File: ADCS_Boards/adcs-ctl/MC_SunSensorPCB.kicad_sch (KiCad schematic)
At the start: 104 parts, among them J1 PC104_Connector, J2 PPTC062LJBN-RC, J3 Conn_01x03_Female, Q3 20V/0.2A/8MHz/1.2Ω/1Vth, Q4 20V/0.2A/8MHz/1.2Ω/1Vth, U1 9DoF IMU, U10 LM324N, U11 LM324N, U12 LM324N, U13 LM324N, U14 1.8V/100mA, U15 STM32F103RET6, U16 MR25H10MDF, U17 1825232-1, U2 BU33SA5WGWZ-E2, U3 9DoF IMU, U4 DF13-7P-1.25DS(20), U5 DF13-7P-1.25DS(20), U6 DF13-7P-1.25DS(20), U7 DF13-7P-1.25DS(20), U8 LM358N, U9 CD74HC4067M96, Y1 Crystal_GND24

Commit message: adcs: adcs-ctl: clean up MCU schematic, add 3V3 led
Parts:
- removed C1, C24, C27, C30: 1.0uF, SparkFun_IMU_Breakout_ICM-20948:0603, symbol SparkFun_IMU_Breakout_ICM-20948-eagle-import:1.0UF-0603-16V-10%-X7R
- removed C10, C11, C12, C13, C14, C15, C16, C17, C18, C19, C20, C21, C3, C4, C5, C6: 180pF, Capacitor_SMD:C_0603_1608Metric, symbol Device:C
- removed C2, C32, C34, C35, C36, C37, C38, C7, C8, C9: 100nF, Capacitor_SMD:C_0603_1608Metric, symbol Device:C
- removed C22, C23, C28, C29: 0.1uF, SparkFun_IMU_Breakout_ICM-20948:0603, symbol SparkFun_IMU_Breakout_ICM-20948-eagle-import:0.1UF-0603-25V-5%
- removed C25, C26: 4pF, Capacitor_SMD:C_0603_1608Metric, symbol Device:C
- removed C31: 100nF, STM32_Breakout:CAPC1608X90, symbol STM32_Breakout-rescue:CC0603MRX5R5BB475-CC0603MRX5R5BB475
- removed C33: 10uF, Capacitor_SMD:C_0603_1608Metric, symbol Device:C
- removed C39: 10nF, Capacitor_SMD:C_0603_1608Metric, symbol Device:C
- removed C40, C41: 1uF, Capacitor_SMD:C_0603_1608Metric, symbol Device:C
- removed C42, C43: 10uF, SparkFun_IMU_Breakout_ICM-20948:0603, symbol SparkFun_IMU_Breakout_ICM-20948-eagle-import:1.0UF-0603-16V-10%-X7R
- removed D1: RED, SparkFun_IMU_Breakout_ICM-20948:LED-0603, symbol SparkFun_IMU_Breakout_ICM-20948-eagle-import:LED-RED0603
- removed D3: RED, LED_SMD:LED_0603_1608Metric_Pad1.05x0.95mm_HandSolder, symbol Device:LED_Small
- removed FB1: 100R @ 100 MHz, STM32_Breakout:INDUC1607X60N, symbol Device:Ferrite_Bead_Small
- removed FB2: FerriteBead, Inductor_SMD:L_0603_1608Metric, symbol Device:FerriteBead
- removed H1, H2, H3, H4: MountingHole_Pad, MountingHole:MountingHole_3.2mm_M3_Pad_TopBottom, symbol Mechanical:MountingHole_Pad
- removed J1: PC104_Connector, pc104-connector:pc104-connector, symbol qset-connector-library:PC104_Connector
- removed J2: PPTC062LJBN-RC, Connector_PinSocket_2.54mm:PinSocket_2x06_P2.54mm_Horizontal, symbol ADCS_Symbols:PPTC062LJBN-RC
- removed J3: Conn_01x03_Female, Footprints_QSAT:1x3_Connector_Female, symbol Connector:Conn_01x03_Female
- removed Q3, Q4: 20V/0.2A/8MHz/1.2Ω/1Vth, SparkFun_IMU_Breakout_ICM-20948:SOT-416FL, symbol SparkFun_IMU_Breakout_ICM-20948-eagle-import:MOSFET-NCH-RE1C002UN
- removed R10, R11, R12, R13, R14, R15, R16, R17, R18, R19, R20, R21, R22, R23, R24, R9: 5.76k, Resistor_SMD:R_0603_1608Metric, symbol Device:R
- removed R2: 10k, Resistor_SMD:R_0603_1608Metric, symbol Device:R
- removed R26, R27, R28, R29: 2.2k, SparkFun_IMU_Breakout_ICM-20948:0402-TIGHT, symbol SparkFun_IMU_Breakout_ICM-20948-eagle-import:2.2KOHM-0402T-1/16W-1%
- removed R36: 220, SparkFun_IMU_Breakout_ICM-20948:0603, symbol SparkFun_IMU_Breakout_ICM-20948-eagle-import:220OHM-0603-1/10W-1%
- removed R53: 2k2, STM32_Breakout:RESC1607X60N, symbol STM32_Breakout-rescue:R0603-OBC_Libary
- removed R54, R55: 10k, STM32_Breakout:RESC1607X60N, symbol STM32_Breakout-rescue:R0603-OBC_Libary
- removed R7: 1Meg, Resistor_SMD:R_0603_1608Metric, symbol Device:R
- removed R8: 2Meg, Resistor_SMD:R_0603_1608Metric, symbol Device:R
- removed S1: TL3305CF260QG, Footprints_QSAT:SW_TL3305CF260QG, symbol ADCS_Symbols:TL3305CF260QG
- removed TP1: 1.8V, SparkFun_IMU_Breakout_ICM-20948:PAD.03X.03, symbol SparkFun_IMU_Breakout_ICM-20948-eagle-import:TEST-POINT3
- removed TP2: 3V3, SparkFun_IMU_Breakout_ICM-20948:PAD.03X.03, symbol SparkFun_IMU_Breakout_ICM-20948-eagle-import:TEST-POINT3
- removed U1, U3: 9DoF IMU, SparkFun_IMU_Breakout_ICM-20948:QFN24-3X3, symbol SparkFun_IMU_Breakout_ICM-20948-eagle-import:ICM-20948
- removed U10, U11, U12, U13: LM324N, Footprints_QSAT:Op-Amp, symbol UpdatedControllerBoardSchematic-rescue:Op-Amp
- removed U14: 1.8V/100mA, SparkFun_IMU_Breakout_ICM-20948:SC70, symbol SparkFun_IMU_Breakout_ICM-20948-eagle-import:V_REG_SP6214-1.8V
- removed U15: STM32F103RET6, Footprints_QSAT:QFP50P1200X1200X160-64N, symbol ADCS_Symbols:STM32F103RET6
- removed U16: MR25H10MDF, STM32_Breakout:SON65P300X300X95-8N, symbol STM32_Breakout-rescue:MR25H10MDF-MRAM_Symbol
- removed U17: 1825232-1, Footprints_QSAT:1825232-1, symbol ADCS_Symbols:1825232-1
- removed U2: BU33SA5WGWZ-E2, Footprints_QSAT:BU33SA5WGWZ-E2, symbol qsat5to3.3-rescue:BU33SA5WGWZ-E2-qsat-symb
- removed U4, U5, U6, U7: DF13-7P-1.25DS(20), Connector_Hirose:Hirose_DF13-07P-1.25DS_1x07_P1.25mm_Horizontal, symbol ADCS_Symbols:DF13-4P-1.25DS(20)
- removed U8: LM358N, Footprints_QSAT:DIP794W45P254L959H508Q8, symbol LM358:LM358
- removed U9: CD74HC4067M96, Footprints_QSAT:SOIC127P1030X265-24N, symbol Mux16_1:CD74HC4067M96
- removed Y1: Crystal_GND24, Crystal:Crystal_SMD_3225-4Pin_3.2x2.5mm, symbol Device:Crystal_GND24
- added C?: 1.0uF, Resistor_SMD:R_0603_1608Metric, symbol SparkFun_IMU_Breakout_ICM-20948-eagle-import:1.0UF-0603-16V-10%-X7R
- added C? (x4): 0.1uF, Capacitor_SMD:C_0603_1608Metric, symbol SparkFun_IMU_Breakout_ICM-20948-eagle-import:0.1UF-0603-25V-5%
- added C? (x16): 180pF, Capacitor_SMD:C_0603_1608Metric, symbol Device:C
- added C?: 10uF, Capacitor_SMD:C_0603_1608Metric, symbol Device:C
- added C? (x2): 10uF, SparkFun_IMU_Breakout_ICM-20948:0603, symbol SparkFun_IMU_Breakout_ICM-20948-eagle-import:1.0UF-0603-16V-10%-X7R
- added C? (x2): 4pF, Capacitor_SMD:C_0603_1608Metric, symbol Device:C
- added C? (x10): 100nF, Capacitor_SMD:C_0603_1608Metric, symbol Device:C
- added C? (x2): 1uF, Capacitor_SMD:C_0603_1608Metric, symbol Device:C
- added C?: 10nF, Capacitor_SMD:C_0603_1608Metric, symbol Device:C
- added C?: 100nF, STM32_Breakout:CAPC1608X90, symbol STM32_Breakout-rescue:CC0603MRX5R5BB475-CC0603MRX5R5BB475
- added C? (x2): 1.0uF, Capacitor_SMD:C_0603_1608Metric, symbol SparkFun_IMU_Breakout_ICM-20948-eagle-import:1.0UF-0603-16V-10%-X7R
- added C?: 10uF, Capacitor_SMD:C_0603_1608Metric, symbol SparkFun_IMU_Breakout_ICM-20948-eagle-import:1.0UF-0603-16V-10%-X7R
- added D? (x2): RED, LED_SMD:LED_0603_1608Metric, symbol SparkFun_IMU_Breakout_ICM-20948-eagle-import:LED-RED0603
- added D?: RED, LED_SMD:LED_0603_1608Metric_Pad1.05x0.95mm_HandSolder, symbol Device:LED_Small
- added FB?: 100R @ 100 MHz, STM32_Breakout:INDUC1607X60N, symbol Device:Ferrite_Bead_Small
- added FB?: FerriteBead, Inductor_SMD:L_0603_1608Metric, symbol Device:FerriteBead
- added H? (x4): MountingHole_Pad, MountingHole:MountingHole_3.2mm_M3_Pad_TopBottom, symbol Mechanical:MountingHole_Pad
- added J?: PPTC062LJBN-RC, Connector_PinSocket_2.54mm:PinSocket_2x06_P2.54mm_Horizontal, symbol ADCS_Symbols:PPTC062LJBN-RC
- added J?: PC104_Connector, pc104-connector:pc104-connector, symbol qset-connector-library:PC104_Connector
- added J?: Conn_01x03_Female, Footprints_QSAT:1x3_Connector_Female, symbol Connector:Conn_01x03_Female
- added Q? (x2): 20V/0.2A/8MHz/1.2Ω/1Vth, SparkFun_IMU_Breakout_ICM-20948:SOT-416FL, symbol SparkFun_IMU_Breakout_ICM-20948-eagle-import:MOSFET-NCH-RE1C002UN
- added R? (x2): 2k2, Resistor_SMD:R_0603_1608Metric, symbol SparkFun_IMU_Breakout_ICM-20948-eagle-import:220OHM-0603-1/10W-1%
- added R? (x4): 2.2k, SparkFun_IMU_Breakout_ICM-20948:0402-TIGHT, symbol SparkFun_IMU_Breakout_ICM-20948-eagle-import:2.2KOHM-0402T-1/16W-1%
- added R? (x16): 5.76k, Resistor_SMD:R_0603_1608Metric, symbol Device:R
- added R?: 2Meg, Resistor_SMD:R_0603_1608Metric, symbol Device:R
- added R?: 1Meg, Resistor_SMD:R_0603_1608Metric, symbol Device:R
- added R?: 10k, Resistor_SMD:R_0603_1608Metric, symbol Device:R
- added R?: 2k2, STM32_Breakout:RESC1607X60N, symbol STM32_Breakout-rescue:R0603-OBC_Libary
- added R?: 10k, STM32_Breakout:RESC1607X60N, symbol STM32_Breakout-rescue:R0603-OBC_Libary
- added R?: 10k, Resistor_SMD:R_0603_1608Metric, symbol STM32_Breakout-rescue:R0603-OBC_Libary
- added S?: TL3305CF260QG, Footprints_QSAT:SW_TL3305CF260QG, symbol ADCS_Symbols:TL3305CF260QG
- added TP?: 1V8, TestPoint:TestPoint_THTPad_2.0x2.0mm_Drill1.0mm, symbol SparkFun_IMU_Breakout_ICM-20948-eagle-import:TEST-POINT3
- added TP?: 3V3, TestPoint:TestPoint_THTPad_2.0x2.0mm_Drill1.0mm, symbol SparkFun_IMU_Breakout_ICM-20948-eagle-import:TEST-POINT3
- added U?: MR25H10MDF, STM32_Breakout:SON65P300X300X95-8N, symbol STM32_Breakout-rescue:MR25H10MDF-MRAM_Symbol
- added U? (x4): LM324N, Footprints_QSAT:Op-Amp, symbol UpdatedControllerBoardSchematic-rescue:Op-Amp
- added U?: 1825232-1, Footprints_QSAT:1825232-1, symbol ADCS_Symbols:1825232-1
- added U? (x4): DF13-7P-1.25DS(20), Connector_Hirose:Hirose_DF13-07P-1.25DS_1x07_P1.25mm_Horizontal, symbol ADCS_Symbols:DF13-4P-1.25DS(20)
- added U?: STM32F103RET6, Footprints_QSAT:QFP50P1200X1200X160-64N, symbol ADCS_Symbols:STM32F103RET6
- added U?: BU33SA5WGWZ-E2, qset-footprints:BU33SA5WGWZ-E2, symbol qsat5to3.3-rescue:BU33SA5WGWZ-E2-qsat-symb
- added U?: CD74HC4067M96, Footprints_QSAT:SOIC127P1030X265-24N, symbol Mux16_1:CD74HC4067M96
- added U? (x2): 9DoF IMU, SparkFun_IMU_Breakout_ICM-20948:QFN24-3X3, symbol SparkFun_IMU_Breakout_ICM-20948-eagle-import:ICM-20948
- added U?: 1.8V/100mA, SparkFun_IMU_Breakout_ICM-20948:SC70, symbol SparkFun_IMU_Breakout_ICM-20948-eagle-import:V_REG_SP6214-1.8V
- added U?: LM358N, Footprints_QSAT:DIP794W45P254L959H508Q8, symbol LM358:LM358
- added Y?: Crystal_GND24, Crystal:Crystal_SMD_3225-4Pin_3.2x2.5mm, symbol Device:Crystal_GND24
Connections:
- net +3.3VA: now also C?.1, C?.1, FB?.1, U?.13 (VDDA)
- net +3V3: now also C?.1, C?.1, C?.1, C?.1, C?.1, C?.1, C?.1, C?.2, D?.2 (A), D?.A, FB?.1, FB?.2, J?.7, R?.1, R?.2, R?.2, R?.2, TP?.P$1 (1), U?.1 (VBAT), U?.19 (VDD_4), U?.3, U?.32 (VDD_1), U?.48 (VDD_2), U?.64 (VDD_3), U?.~ (Vout)
- net +5V: now also C?.1, C?.1, C?.1, C?.1, C?.1, C?.1, J?.78 (H1-26), U?.1 (IN), U?.24 (VCC), U?.3 (EN), U?.3 (Input), U?.4, U?.4, U?.4, U?.4, U?.8 (V+)
- net 1.8V: now also C?.1, C?.1, C?.1, C?.1, C?.1, D?.A, Q?.1 (G), Q?.1 (G), R?.2, R?.2, TP?.P$1 (1), U?.13 (VDD), U?.13 (VDD), U?.5 (OUT), U?.8 (VDDIO), U?.8 (VDDIO), U?.9 (AD0/SDO)
- net BOOT0: now also R?.2, U?.60 (BOOT0)
- net GND: now also C?.1, C?.2, C?.2, C?.2, C?.2, C?.2, C?.2, C?.2, C?.2, C?.2, C?.2, C?.2, C?.2, C?.2, C?.2, C?.2, C?.2, C?.2, C?.2, C?.2, C?.2, C?.2, C?.2, C?.2, C?.2, C?.2, C?.2, J?.100 (H2-48), J?.61 (H2-9), J?.66 (H1-14), J?.69 (H2-17), J?.73 (H2-21), J?.74 (H1-22), J?.8, J?.81 (H2-29), J?.82 (H1-30), J?.84 (H1-32), J?.99 (H2-47), R?.1, R?.1, R?.2, R?.2, S?.3, S?.4, U?.1, U?.1 (GND), U?.10, U?.10, U?.10, U?.10, U?.11, U?.11, U?.11, U?.11, U?.12, U?.12, U?.12, U?.12, U?.12 (GND), U?.12 (VSSA), U?.18 (GND), U?.18 (GND), U?.18 (VSS_4), U?.2, U?.2, U?.2, U?.2, U?.2 (GND), U?.20 (GND), U?.20 (GND), U?.3, U?.3, U?.3, U?.3, U?.31 (VSS_1), U?.4, U?.4, U?.4, U?.4, U?.4 (GND), U?.4 (VSS), U?.47 (VSS_2), U?.5, U?.5, U?.5, U?.5, U?.6, U?.6, U?.6, U?.6, U?.63 (VSS_3), U?.9 (AD0/SDO), U?.9 (Sink), Y?.2, Y?.4
- net GPIO1: now also R?.2, U?.24 (PC4/ADC12_IN14), U?.7 (HOLD)
- net GPIO2: now also R?.1, U?.25 (PC5/ADC12_IN15), U?.3 (WP)
- net IMU_SCL: now also Q?.3 (D), R?.1, U?.39 (PC8/TIM8_CH3/SDIO_D0/TIM3_CH3)
- net IMU_SDA: now also Q?.3 (D), R?.1, U?.40 (PC9/TIM8_CH4/SDIO_D1/TIM3_CH4)
- net MuxEnable: now also U?.14 (PA0-WKUP/USART2_CTS/ADC123_IN0/TIM2_CH1_ETR/TIM5_CH1/TIM8_ETR), U?.15 (~{E})
- net MuxOut: now also U?.1, U?.2, U?.21 (PA5/SPI1_SCK/DAC_OUT2/ADC12_IN5)
- net MuxOut_1: now also R?.1, U?.1 (COM_I/O)
- net MuxS0: now also U?.10 (S0), U?.15 (PA1/USART2_RTS/ADC123_IN1/TIM5_CH2/TIM2_CH2)
- net MuxS1: now also U?.11 (S1), U?.16 (PA2/USART2_TX/TIM5_CH3/ADC123_IN2/TIM2_CH3)
- net MuxS2: now also U?.14 (S2), U?.17 (PA3/USART2_RX/TIM5_CH4/ADC123_IN3/TIM2_CH4)
- net MuxS3: now also U?.13 (S3), U?.20 (PA4/SPI1_NSS/USART2_CK/DAC_OUT1/ADC12_IN4)
- net NRST: now also C?.1, S?.1, S?.2, U?.7 (NRST)
- net PA10: now also J?.20 (H1-20), U?.43 (PA10/USART1_RX/TIM1_CH3)
- net PA11: now also J?.21 (H1-21), U?.44 (PA11/USART1_CTS/USBDMCAN_RX/TIM1_CH4)
- net PA12: now also J?.22 (H1-22), U?.45 (PA12/USART1_RTS/USBDP/CAN_TX/TIM1_ETR)
- net PA15: now also J?.25 (H1-25), U?.50 (PA15/SPI3_NSS/I2S3_WS)
- net PA6: now also J?.16 (H1-16), U?.22 (PA6/SPI1_MISO/TIM8_BKIN/ADC12_IN6/TIM3_CH1)
- net PA7: now also J?.17 (H1-17), U?.23 (PA7/SPI1_MOSI/TIM8_CH1N/ADC12_IN7/TIM3_CH2)
- net PA8: now also J?.18 (H1-18), U?.41 (PA8/USART1_CK/TIM1_CH1/MCO)
- net PA9: now also J?.19 (H1-19), U?.42 (PA9/USART1_TX/TIM1_CH2)
- net PB0: now also J?.24 (H1-24), U?.26 (PB0/ADC12_IN8/TIM3_CH3/TIM8_CH2N)
- net PB1: now also J?.42 (H1-42), U?.27 (PB1/ADC12_IN9/TIM3_CH4/TIM8_CH3N)
- net PB10: now also J?.23 (H1-23), U?.29 (PB10/I2C2_SCL/USART3_TX/TIM2_CH3)
- net PB11: now also J?.51 (H1-51), U?.30 (PB11/2C2_SDA/USART3_RX/TIM2_CH4)
- net PB12: now also J?.26 (H1-26), U?.33 (PB12/SPI2_NSS/I2S2_WS/I2C2_SMBA/USART3_CK/TIM1_BKIN)
- net PB13: now also J?.27 (H1-27), U?.34 (PB13/SPI2_SCK/I2S2_CK/USART3_CTS/TIM1_CH1N)
- net PB14: now also J?.37 (H1-37), U?.35 (PB14/SPI2_MISO/TIM1_CH2N/USART3_RTS)
- net PB15: now also J?.38 (H1-38), U?.36 (PB15/SPI2_MOSI/I2S2_SD/TIM1_CH3N)
- net PB2: now also U?.28 (PB2//BOOT1)
- net PB4: now also J?.50 (H1-50), U?.56 (PB4/SPI3_MISO/TIM3_CH1/SPI1_MISO)
- net PB5: now also U?.57 (PB5/TIM3_CH2/SPI1_MOSI/)
- net PB8: now also J?.52 (H1-52), U?.61 (PB8/TIM4_CH3/SDIO_D4/I2C1_SCL/CAN_RX)
- net PB9: now also U?.62 (PB9/TIM4_CH4/SDIO_D5/I2C1_SDA/CAN_TX)
- net PC10: now also J?.5 (H1-5), U?.51 (PC10/UART4_TX/SDIO_D2/USART3_TX)
- net PC11: now also J?.44 (H1-44), U?.52 (PC11/UART4_RX/SDIO_D3/USART3_RX)
- net PC12: now also J?.45 (H1-45), U?.53 (PC12/UART5_TX/SDIO_CK/USART3_CK)
- net PC13: now also J?.46 (H1-46), U?.2 (PC13-TAMPER-RTC)
- net PC14: now also J?.47 (H1-47), U?.3 (PC14-OSC32_IN)
- net PC15: now also J?.48 (H1-48), U?.4 (PC15-OSC32_OUT)
- net PC6: now also J?.39 (H1-39), U?.37 (PC6/I2S2_MCK/TIM8_CH1/SDIO_D6/TIM3_CH1)
- net PC7: now also J?.40 (H1-40), U?.38 (PC7/I2S3_MCK/TIM8_CH2/SDIO_D7/TIM3_CH2)
- net PD1_O1: now also C?.2, R?.2, U?.1, U?.2
- net PD1_O2: now also C?.2, R?.2, U?.1, U?.2
- net PD1_O3: now also C?.2, R?.2, U?.1, U?.2
- net PD1_O4: now also C?.2, R?.2, U?.1, U?.2
- net PD2: now also J?.49 (H1-49), U?.54 (PD2/TIM3_ETR/UART5_RX/SDIO_CMD)
- net PD2_O1: now also C?.2, R?.1, U?.3, U?.6
- net PD2_O2: now also C?.2, R?.1, U?.3, U?.6
- net PD2_O3: now also C?.2, R?.1, U?.3, U?.6
- net PD2_O4: now also C?.2, R?.1, U?.3, U?.6
- net PD3_O1: now also C?.2, R?.2, U?.13, U?.5
- net PD3_O2: now also C?.2, R?.2, U?.13, U?.5
- net PD3_O3: now also C?.2, R?.2, U?.13, U?.5
- net PD3_O4: now also C?.2, R?.2, U?.13, U?.5
- net PD4_O1: now also C?.1, R?.1, U?.7, U?.9
- net PD4_O2: now also C?.1, R?.1, U?.7, U?.9
- net PD4_O3: now also C?.1, R?.1, U?.7, U?.9
- net PD4_O4: now also C?.1, R?.1, U?.7, U?.9
- net SPI1_MISO: now also U?.11 (PC3/ADC123_IN13), U?.2 (SO)
- net SPI1_MOSI: now also U?.5 (SI), U?.9 (PC1/ADC123_IN11)
- net SPI1_NSS: now also U?.1 (CS), U?.10 (PC2/ADC123_IN12)
- net SPI1_SCK: now also U?.6 (SCK), U?.8 (PC0/ADC123_IN10)
- net SW_BOOT0: now also R?.1, U?.2
- net SYS_JTCK-SWCLK: now also J?.2 (Pin_2), U?.49 (PA14/JTCKSWCLK)
- net SYS_JTDO-TRACESWO: now also J?.3 (Pin_3), U?.55 (PB3/SPI3_SCK/I2S3_CK/TRACESWO/TIM2_CH2/SPI1_SCK)
- net SYS_JTMS-SWDIO: now also J?.1 (Pin_1), U?.46 (PA13/JTMSSWDIO)
- new net: D?.C, R?.2 (x2)
- new net: C?.1, FB?.2, U?.8 (VDD)
- new net: C?.1, R?.2, U?.7, U?.8 (I1)
- new net: C?.1, R?.1, U?.14, U?.3 (I6)
- new net: C?.2, R?.2, U?.20 (I11), U?.8
- new net: R?.1, R?.2, U?.3
- new net: C?.1, R?.1, U?.1, U?.19 (I12)
- new net: C?.1, R?.1, U?.14, U?.21 (I10)
- new net: C?.1, R?.2, U?.4 (I5), U?.7
- new net: C?.1, R?.1, U?.1, U?.5 (I4)
- new net: C?.2, R?.2, U?.2 (I7), U?.8
- new net: C?.1, R?.1, U?.14, U?.17 (I14)
- new net: C?.2, R?.2, U?.16 (I15), U?.8
- new net: C?.1, U?.5 (PD0-OSC_IN/FSMC_D2/CAN_RX), Y?.3
- new net: C?.1, U?.6 (PD1-OSC_OUT/FSMC_D3/CAN_TX), Y?.1
- new net: C?.1, R?.2, U?.18 (I13), U?.7
- new net: C?.1, R?.1, U?.14, U?.7 (I2)
- new net: C?.1, R?.2, U?.22 (I9), U?.7
- new net: C?.2, R?.2, U?.6 (I3), U?.8
- new net: C?.1, R?.1, U?.1, U?.9 (I0)
- new net: C?.1, R?.1, U?.1, U?.23 (I8)
- new net: C?.1, U?.10 (REGOUT) (x2)
- new net: D?.1 (K), R?.1
- new net I2C1_SCL: J?.11, J?.43 (H1-43), U?.58 (PB6/I2C1_SCL/TIM4_CH1/USART1_TX)
- new net I2C1_SDA: J?.12, J?.41 (H1-41), U?.59 (PB7/I2C1_SDA/FSMC_NADV/TIM4_CH2/USART1_RX)
- new net IMU_SCL_1V8: Q?.2 (S), R?.1, U?.23 (SCL/SCLK), U?.23 (SCL/SCLK)
- new net IMU_SDA_1V8: Q?.2 (S), R?.1, U?.24 (SDA/SDI), U?.24 (SDA/SDI)
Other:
- note added: "1V8 I2C Pullups"
- note added: "1V8 Power Generation"
- note added: "3V3 Power Generation"
- note added: "MCU - STM32F103RET6"
- note added: "PMOD Test Connector"
- note added: "SWD / Programming Header"
- note removed: "1v8 Power Generation"
- note removed: "3v3 Power Generation"
- note removed: "Crystal Oscillator"
- note removed: "I2C Pullups"
- note removed: "PMOD"
- note removed: "SWD"

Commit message: adcs: adcs-ctl: change boot switch to standard footprint and symbol
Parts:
- removed U?: 1825232-1, Footprints_QSAT:1825232-1, symbol ADCS_Symbols:1825232-1
- added SW1: SW_SPDT, Button_Switch_SMD:SW_SPDT_PCM12, symbol Switch:SW_SPDT
- gave numbers to parts that had none: 105
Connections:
- net +3V3: now also SW1.3 (C)
- net GND: now also SW1.1 (A)
- net SW_BOOT0: now also SW1.2 (B)

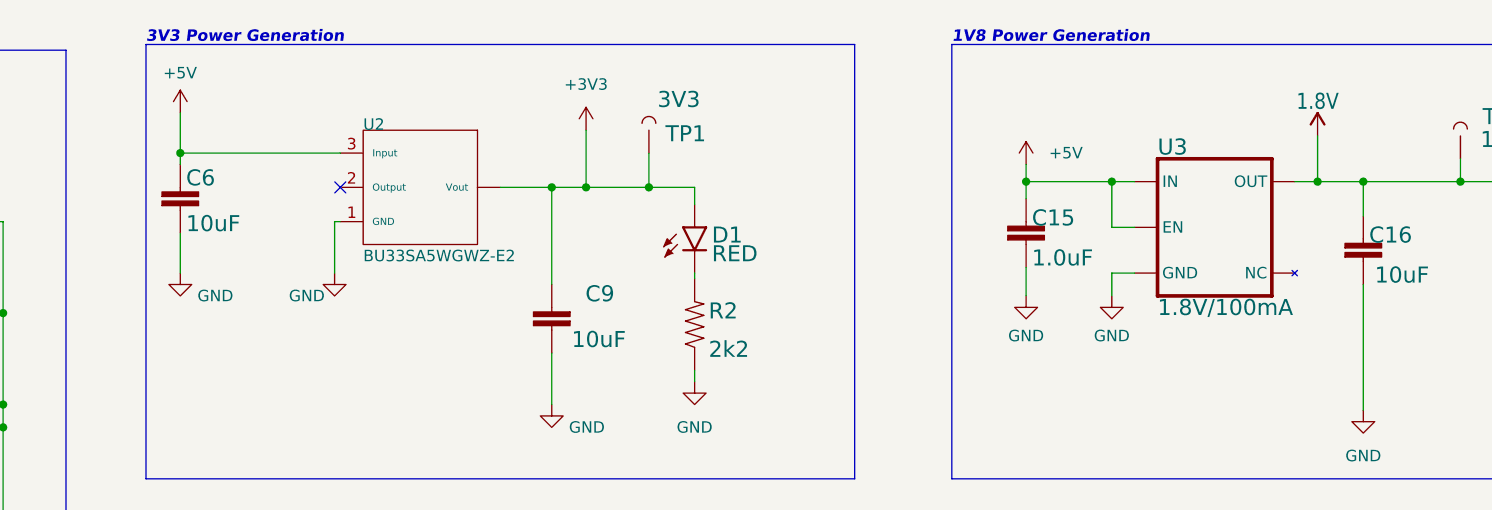
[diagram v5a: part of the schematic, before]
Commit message: adcs: adcs-ctl: use AMS1117 regulators
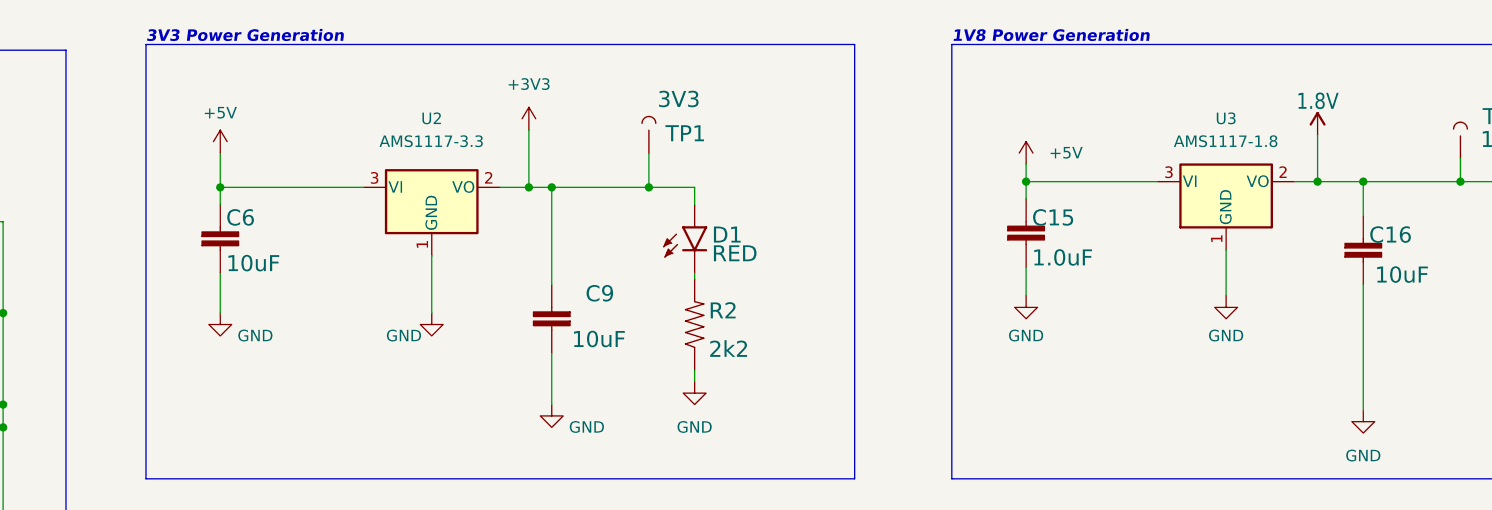
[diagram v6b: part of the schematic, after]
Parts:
- removed U2: BU33SA5WGWZ-E2, qset-footprints:BU33SA5WGWZ-E2, symbol qsat5to3.3-rescue:BU33SA5WGWZ-E2-qsat-symb
- removed U3: 1.8V/100mA, SparkFun_IMU_Breakout_ICM-20948:SC70, symbol SparkFun_IMU_Breakout_ICM-20948-eagle-import:V_REG_SP6214-1.8V
- added U2: AMS1117-3.3, Package_TO_SOT_SMD:SOT-223-3_TabPin2, symbol Regulator_Linear:AMS1117-3.3
- added U3: AMS1117-1.8, Package_TO_SOT_SMD:SOT-223-3_TabPin2, symbol Regulator_Linear:AMS1117-1.8
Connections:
- net +3V3: now also U2.2 (VO)
- net +5V: now also U2.3 (VI), U3.3 (VI)
- net 1.8V: now also U3.2 (VO)
- net GND: now also U2.1 (GND), U3.1 (GND)
- no-connect marks 78 -> 77
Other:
- moved on the sheet: C6

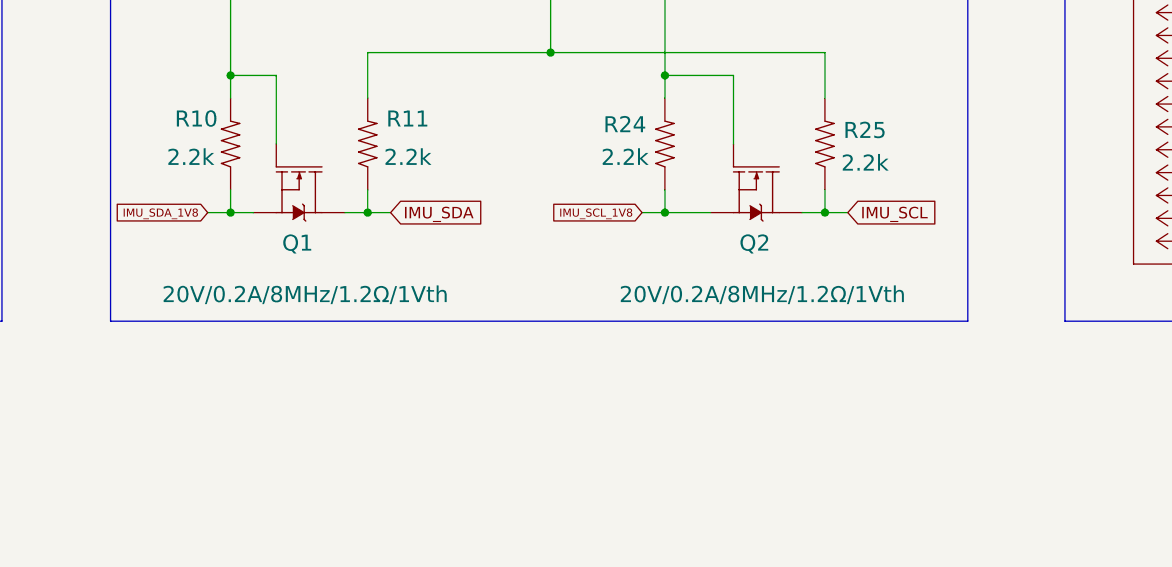
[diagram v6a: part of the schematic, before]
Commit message: adcs: adcs-ctl: use re1c002unctl transistors over SparkFun transistors
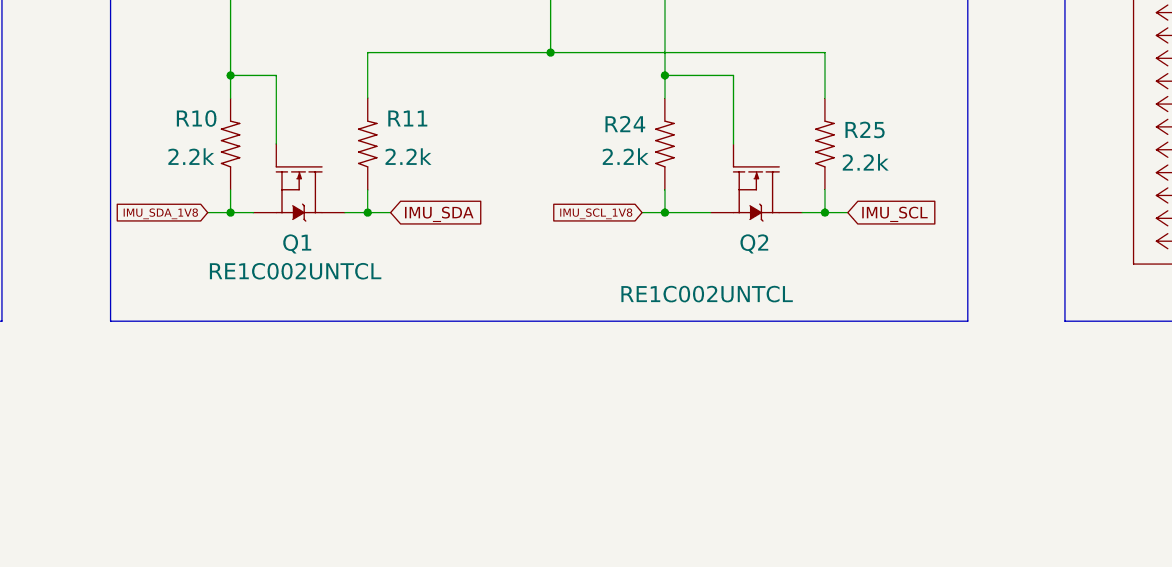
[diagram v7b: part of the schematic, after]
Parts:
- Q1, Q2: value 20V/0.2A/8MHz/1.2Ω/1Vth -> RE1C002UNTCL; footprint SparkFun_IMU_Breakout_ICM-20948:SOT-416FL -> qset-footprints:RE1C002UNTCL
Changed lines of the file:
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@@
       (effects (font (size 1.778 1.778)) (justify left bottom))
     )
-    (property "Value" "20V/0.2A/8MHz/1.2Ω/1Vth" (id 1) (at 357.505 66.04 90)
+    (property "Value" "RE1C002UNTCL" (id 1) (at 362.585 63.5 90)
       (effects (font (size 1.778 1.778)) (justify left bottom))
     )
-    (property "Footprint" "SparkFun_IMU_Breakout_ICM-20948:SOT-416FL" (id 2) (at 372.745 53.34 0)
+    (property "Footprint" "qset-footprints:RE1C002UNTCL" (id 2) (at 372.745 53.34 0)
       (effects (font (size 1.27 1.27)) hide)
     )
@@
       (effects (font (size 1.778 1.778)) (justify left bottom))
     )
-    (property "Value" "20V/0.2A/8MHz/1.2Ω/1Vth" (id 1) (at 408.305 66.04 90)
+    (property "Value" "RE1C002UNTCL" (id 1) (at 408.305 66.04 90)
       (effects (font (size 1.778 1.778)) (justify left bottom))
     )
-    (property "Footprint" "SparkFun_IMU_Breakout_ICM-20948:SOT-416FL" (id 2) (at 423.545 53.34 0)
+    (property "Footprint" "qset-footprints:RE1C002UNTCL" (id 2) (at 423.545 53.34 0)
       (effects (font (size 1.27 1.27)) hide)
     )
@@
     )
     (path "/c3b4cda1-0c94-458d-8295-e36b579c60f5"
-      (reference "Q1") (unit 1) (value "20V/0.2A/8MHz/1.2Ω/1Vth") (footprint "SparkFun_IMU_Breakout_ICM-20948:SOT-416FL")
+      (reference "Q1") (unit 1) (value "RE1C002UNTCL") (footprint "qset-footprints:RE1C002UNTCL")
     )
     (path "/fd63de2a-d1fa-4d62-ae82-a9332a975f37"
-      (reference "Q2") (unit 1) (value "20V/0.2A/8MHz/1.2Ω/1Vth") (footprint "SparkFun_IMU_Breakout_ICM-20948:SOT-416FL")
+      (reference "Q2") (unit 1) (value "RE1C002UNTCL") (footprint "qset-footprints:RE1C002UNTCL")
     )
     (path "/8d780721-f9df-4182-969c-15350fd7dc18"

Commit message: adcs: adcs-ctl: partial clean up of sun sensor schematic
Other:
- moved on the sheet: C17, C18, C19, C20, C21, C22, C23, C24, C25, C26, C27, C28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
